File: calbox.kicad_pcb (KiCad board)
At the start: 2 copper layers, 101.6 x 76.2 mm, 68 parts, among them P1 BNC, P2 CONN_01X01, P3 CONN_01X01, Q1 Q_NPN_BEC, SW1 SW_Rotary12, SW2 SW_Rotary12, SW3 SW_SPDT, SW4 SW_Rotary12, SW5 SW_DPST_NKK_M2021, U1 74LVC161, U10 74LVC161, U11 74LVC74, U12 74LVC14, U13 LM317_SOT223_4pin, U14 LM317_SOT223_4pin, U2 74LVC161, U3 74LVC161, U4 74LVC161, U5 74LVC00, U6 74LVC161, U7 74LVC161, U8 74LVC00, U9 74LVC74, X1 ACHL_XO

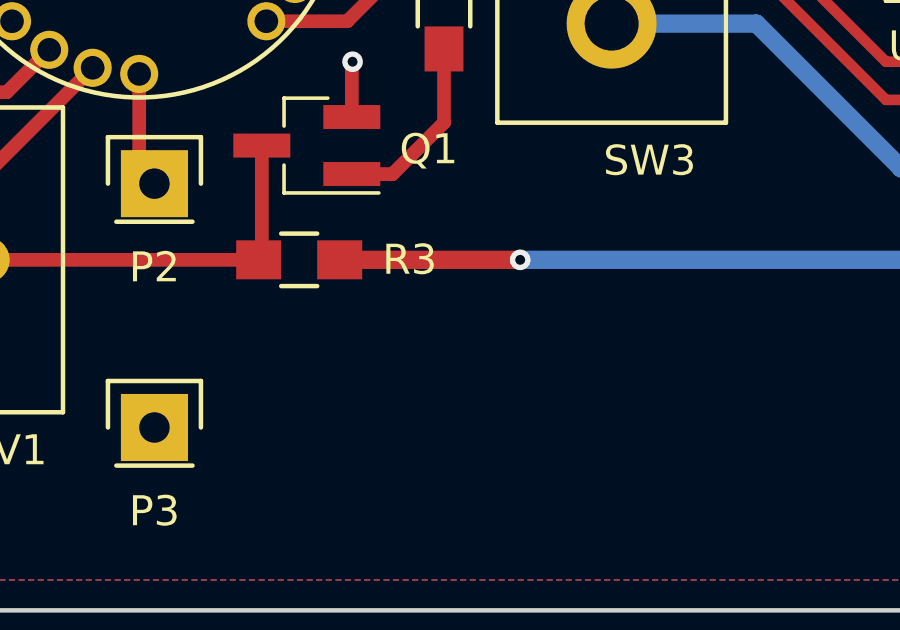
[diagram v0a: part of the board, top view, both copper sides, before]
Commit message: Added bypass capacitor to +12V line
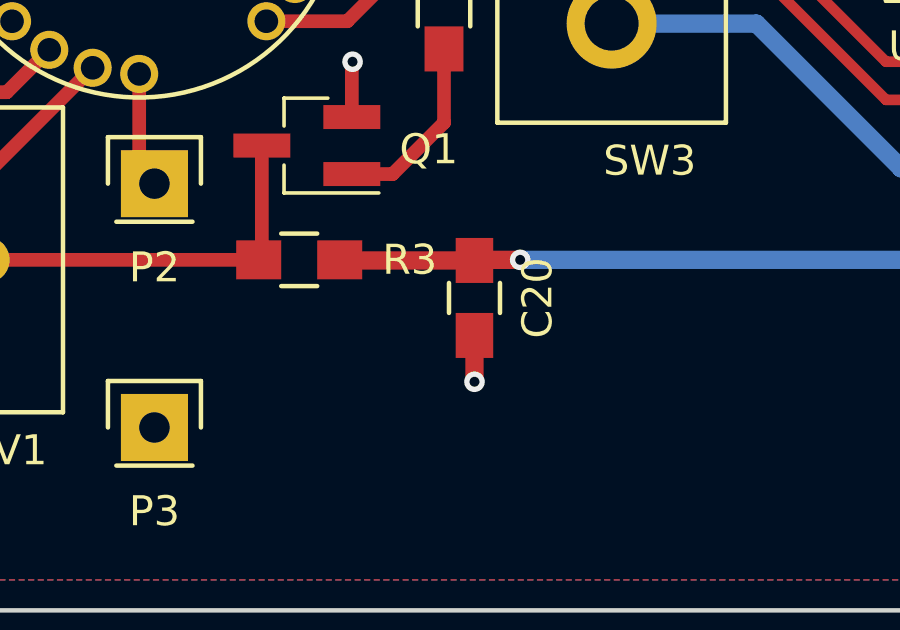
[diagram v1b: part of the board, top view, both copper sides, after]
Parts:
- added C20: 6.8u, Capacitors_SMD:C_0805_HandSoldering, F.Cu at (107.7, 152.1)
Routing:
- net GND: track 129.9 -> 131.5 mm, vias 36 -> 37
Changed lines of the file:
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@@
 (kicad_pcb (version 4) (host pcbnew 4.0.5)
   (general
-    (links 238)
+    (links 240)
     (no_connects 0)
-    (area 65.964999 85.771 169.139239 162.635001)
+    (area 65.964999 86.284999 167.715001 162.635001)
     (thickness 1.6)
     (drawings 4)
-    (tracks 729)
+    (tracks 734)
     (zones 0)
-    (modules 68)
+    (modules 69)
     (nets 99)
   )
@@
   (layers
     (0 F.Cu signal)
-    (31 B.Cu signal)
+    (31 B.Cu signal hide)
     (33 F.Adhes user)
     (35 F.Paste user)
@@
   )
   (setup
-    (last_trace_width 0.3048)
+    (last_trace_width 0.6096)
     (user_trace_width 0.3048)
     (user_trace_width 0.3556)
@@
     )
   )
+  (module Capacitors_SMD:C_0805_HandSoldering (layer F.Cu)
+    (at 107.696 152.146 270)
+    (descr "Capacitor SMD 0805, hand soldering")
+    (tags "capacitor 0805")
+    (attr smd)
+    (fp_text reference C20 (at 0 -2.1 270) (layer F.SilkS)
+      (effects (font (size 1 1) (thickness 0.15)))
+    )
+    (fp_text value 6.8u (at 0 2.1 270) (layer F.Fab)
+      (effects (font (size 1 1) (thickness 0.15)))
+    )
+    (fp_line (start -1 0.625) (end -1 -0.625) (layer F.Fab) (width 0.15))
+    (fp_line (start 1 0.625) (end -1 0.625) (layer F.Fab) (width 0.15))
+    (fp_line (start 1 -0.625) (end 1 0.625) (layer F.Fab) (width 0.15))
+    (fp_line (start -1 -0.625) (end 1 -0.625) (layer F.Fab) (width 0.15))
+    (fp_line (start -2.3 -1) (end 2.3 -1) (layer F.CrtYd) (width 0.05))
+    (fp_line (start -2.3 1) (end 2.3 1) (layer F.CrtYd) (width 0.05))
+    (fp_line (start -2.3 -1) (end -2.3 1) (layer F.CrtYd) (width 0.05))
+    (fp_line (start 2.3 -1) (end 2.3 1) (layer F.CrtYd) (width 0.05))
+    (fp_line (start 0.5 -0.85) (end -0.5 -0.85) (layer F.SilkS) (width 0.15))
+    (fp_line (start -0.5 0.85) (end 0.5 0.85) (layer F.SilkS) (width 0.15))
+    (pad 1 smd rect (at -1.25 0 270) (size 1.5 1.25) (layers F.Cu F.Paste F.Mask)
+      (net 7 +12V))
+    (pad 2 smd rect (at 1.25 0 270) (size 1.5 1.25) (layers F.Cu F.Paste F.Mask)
+      (net 3 GND))
+    (model Capacitors_SMD.3dshapes/C_0805_HandSoldering.wrl
+      (at (xyz 0 0 0))
+      (scale (xyz 1 1 1))
+      (rotate (xyz 0 0 0))
+    )
+  )
   (gr_line (start 167.64 162.56) (end 66.04 162.56) (angle 90) (layer Edge.Cuts) (width 0.15))
   (gr_line (start 167.64 86.36) (end 167.64 162.56) (angle 90) (layer Edge.Cuts) (width 0.15))
@@
   (segment (start 160.147 99.695) (end 159.004 98.552) (width 0.4572) (layer F.Cu) (net 2))
   (segment (start 163.83 99.695) (end 163.83 93.345) (width 0.4572) (layer F.Cu) (net 2))
+  (segment (start 107.696 153.396) (end 107.696 154.94) (width 0.6096) (layer F.Cu) (net 3))
+  (via (at 107.696 154.94) (size 0.6858) (drill 0.3302) (layers F.Cu B.Cu) (net 3))
   (segment (start 144.86 95.885) (end 144.86 98.425) (width 0.6096) (layer F.Cu) (net 3))
   (segment (start 144.86 98.425) (end 146.511 100.076) (width 0.6096) (layer F.Cu) (net 3))
@@
   (segment (start 164.56 119.5) (end 164.44 119.62) (width 0.4572) (layer F.Cu) (net 6))
   (segment (start 161.29 108.966) (end 161.29 109.22) (width 0.4572) (layer F.Cu) (net 6))
+  (segment (start 107.696 150.896) (end 103.224 150.896) (width 0.6096) (layer F.Cu) (net 7))
+  (segment (start 103.224 150.896) (end 103.204 150.876) (width 0.6096) (layer F.Cu) (net 7))
+  (segment (start 109.22 150.876) (end 107.716 150.876) (width 0.6096) (layer F.Cu) (net 7))
+  (segment (start 107.716 150.876) (end 107.696 150.896) (width 0.6096) (layer F.Cu) (net 7))
   (segment (start 158.77 133.35) (end 158.77 136.886) (width 0.6096) (layer F.Cu) (net 7))
-  (segment (start 158.77 136.886) (end 157.988 137.668) (width 0.6096) (layer F.Cu) (net 7))
-  (via (at 157.988 137.668) (size 0.6858) (drill 0.3302) (layers F.Cu B.Cu) (net 7))
-  (segment (start 157.988 137.668) (end 152.908 142.748) (width 0.6096) (layer B.Cu) (net 7))
-  (segment (start 152.908 142.748) (end 148.844 142.748) (width 0.6096) (layer B.Cu) (net 7))
-  (segment (start 148.844 142.748) (end 140.716 150.876) (width 0.6096) (layer B.Cu) (net 7))
-  (segment (start 140.716 150.876) (end 109.22 150.876) (width 0.6096) (layer B.Cu) (net 7))
   (via (at 109.22 150.876) (size 0.6858) (drill 0.3302) (layers F.Cu B.Cu) (net 7))
-  (segment (start 109.22 150.876) (end 103.204 150.876) (width 0.6096) (layer F.Cu) (net 7))
+  (segment (start 140.716 150.876) (end 109.22 150.876) (width 0.6096) (layer B.Cu) (net 7))
+  (segment (start 148.844 142.748) (end 140.716 150.876) (width 0.6096) (layer B.Cu) (net 7))
+  (segment (start 152.908 142.748) (end 148.844 142.748) (width 0.6096) (layer B.Cu) (net 7))
+  (segment (start 157.988 137.668) (end 152.908 142.748) (width 0.6096) (layer B.Cu) (net 7))
+  (via (at 157.988 137.668) (size 0.6858) (drill 0.3302) (layers F.Cu B.Cu) (net 7))
+  (segment (start 158.77 136.886) (end 157.988 137.668) (width 0.6096) (layer F.Cu) (net 7))
   (segment (start 158.14 121.92) (end 158.14 121.056) (width 0.6096) (layer F.Cu) (net 7))
   (segment (start 158.14 121.056) (end 155.448 118.364) (width 0.6096) (layer F.Cu) (net 7))

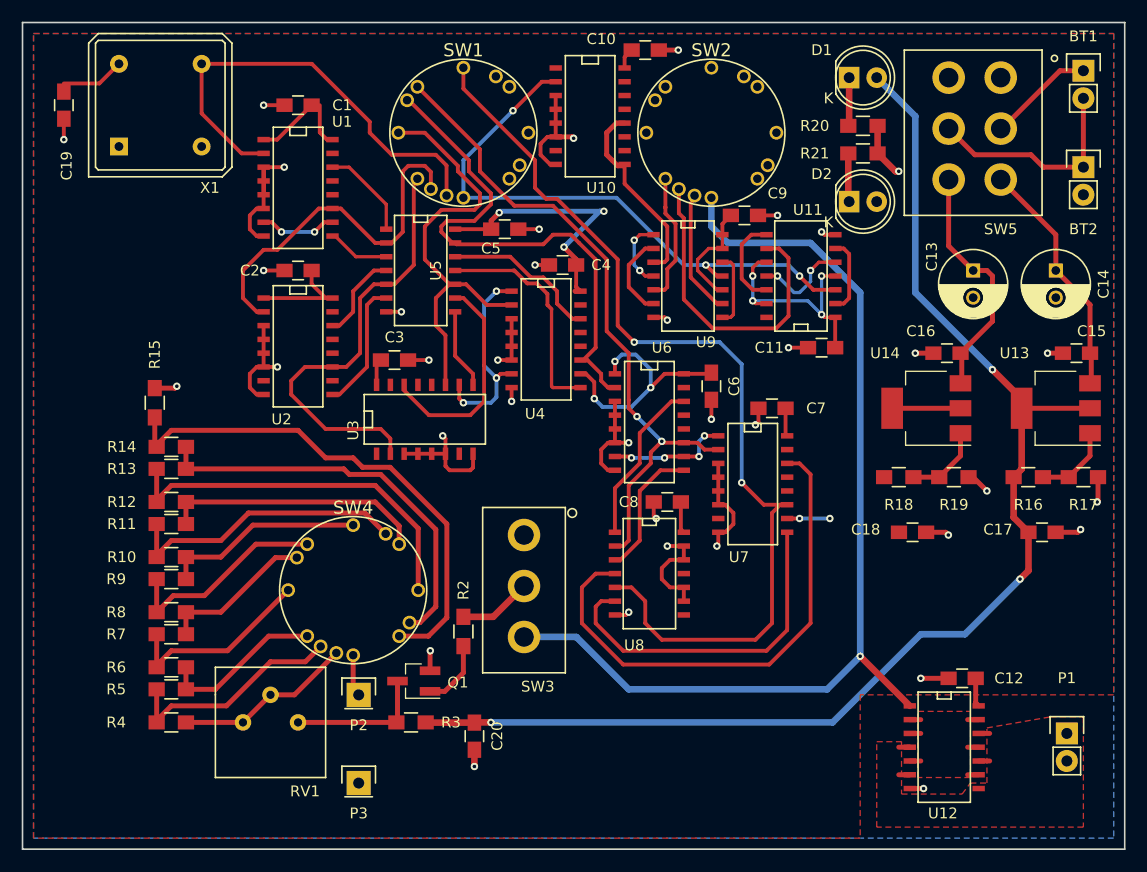
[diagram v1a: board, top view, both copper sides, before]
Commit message: Added testpoints for VCC, 12V, and GND
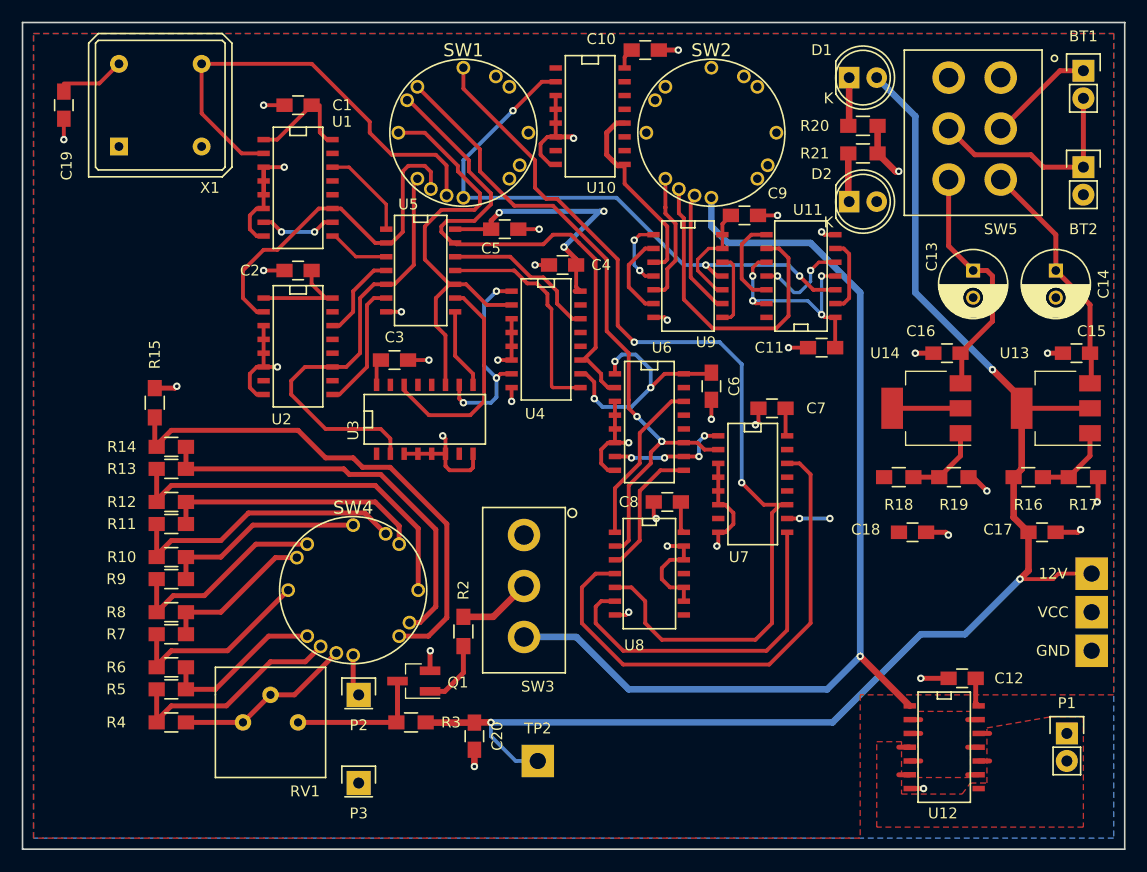
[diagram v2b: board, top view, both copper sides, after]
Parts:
- added 12V: TEST, Measurement_Points:Measurement_Point_Square-TH_Big, F.Cu at (164.6, 137.2)
- added GND: TEST, Measurement_Points:Measurement_Point_Square-TH_Big, F.Cu at (164.6, 144.3)
- added TP2: TEST, Measurement_Points:Measurement_Point_Square-TH_Big, F.Cu at (113.5, 154.4)
- added VCC: TEST, Measurement_Points:Measurement_Point_Square-TH_Big, F.Cu at (164.6, 140.7)
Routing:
- net +12V: track 119.6 -> 132.9 mm
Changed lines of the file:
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@@
 (kicad_pcb (version 4) (host pcbnew 4.0.5)
   (general
-    (links 240)
+    (links 244)
     (no_connects 0)
     (area 65.964999 86.284999 167.715001 162.635001)
     (thickness 1.6)
     (drawings 4)
-    (tracks 734)
+    (tracks 740)
     (zones 0)
-    (modules 69)
+    (modules 73)
     (nets 99)
   )
@@
   (layers
     (0 F.Cu signal)
-    (31 B.Cu signal hide)
+    (31 B.Cu signal)
     (33 F.Adhes user)
     (35 F.Paste user)
@@
   )
   (setup
-    (last_trace_width 0.6096)
+    (last_trace_width 0.3048)
     (user_trace_width 0.3048)
     (user_trace_width 0.3556)
@@
     (tags "CMS SOJ")
     (attr smd)
-    (fp_text reference U5 (at 0 -1.27 270) (layer F.SilkS)
+    (fp_text reference U5 (at -6.096 1.27 360) (layer F.SilkS)
       (effects (font (size 1 1) (thickness 0.15)))
     )
@@
     (descr "Through hole pin header")
     (tags "pin header")
-    (fp_text reference P1 (at 0 -5.1) (layer F.SilkS)
+    (fp_text reference P1 (at 0 -2.794) (layer F.SilkS)
       (effects (font (size 1 1) (thickness 0.15)))
     )
@@
     )
   )
+  (module Measurement_Points:Measurement_Point_Square-TH_Big (layer F.Cu)
+    (at 113.538 154.432)
+    (descr "Mesurement Point, Square, Trough Hole,  3mm x 3mm, Drill 1.5mm,")
+    (tags "Mesurement Point Square Trough Hole 3x3mm Drill 1.5mm")
+    (attr virtual)
+    (fp_text reference TP2 (at 0 -3) (layer F.SilkS)
+      (effects (font (size 1 1) (thickness 0.15)))
+    )
+    (fp_text value TEST (at 0 3) (layer F.Fab)
+      (effects (font (size 1 1) (thickness 0.15)))
+    )
+    (fp_line (start -1.75 -1.75) (end 1.75 -1.75) (layer F.CrtYd) (width 0.05))
+    (fp_line (start 1.75 -1.75) (end 1.75 1.75) (layer F.CrtYd) (width 0.05))
+    (fp_line (start 1.75 1.75) (end -1.75 1.75) (layer F.CrtYd) (width 0.05))
+    (fp_line (start -1.75 1.75) (end -1.75 -1.75) (layer F.CrtYd) (width 0.05))
+    (pad 1 thru_hole rect (at 0 0) (size 3 3) (drill 1.5) (layers *.Cu *.Mask)
+      (net 7 +12V))
+  )
+  (module Measurement_Points:Measurement_Point_Square-TH_Big (layer F.Cu)
+    (at 164.592 144.272)
+    (descr "Mesurement Point, Square, Trough Hole,  3mm x 3mm, Drill 1.5mm,")
+    (tags "Mesurement Point Square Trough Hole 3x3mm Drill 1.5mm")
+    (attr virtual)
+    (fp_text reference GND (at -3.556 0) (layer F.SilkS)
+      (effects (font (size 1 1) (thickness 0.15)))
+    )
+    (fp_text value TEST (at 0 3) (layer F.Fab)
+      (effects (font (size 1 1) (thickness 0.15)))
+    )
+    (fp_line (start -1.75 -1.75) (end 1.75 -1.75) (layer F.CrtYd) (width 0.05))
+    (fp_line (start 1.75 -1.75) (end 1.75 1.75) (layer F.CrtYd) (width 0.05))
+    (fp_line (start 1.75 1.75) (end -1.75 1.75) (layer F.CrtYd) (width 0.05))
+    (fp_line (start -1.75 1.75) (end -1.75 -1.75) (layer F.CrtYd) (width 0.05))
+    (pad 1 thru_hole rect (at 0 0) (size 3 3) (drill 1.5) (layers *.Cu *.Mask)
+      (net 3 GND))
+  )
+  (module Measurement_Points:Measurement_Point_Square-TH_Big (layer F.Cu)
+    (at 164.592 137.16)
+    (descr "Mesurement Point, Square, Trough Hole,  3mm x 3mm, Drill 1.5mm,")
+    (tags "Mesurement Point Square Trough Hole 3x3mm Drill 1.5mm")
+    (attr virtual)
+    (fp_text reference 12V (at -3.556 0) (layer F.SilkS)
+      (effects (font (size 1 1) (thickness 0.15)))
+    )
+    (fp_text value TEST (at 0 3) (layer F.Fab)
+      (effects (font (size 1 1) (thickness 0.15)))
+    )
+    (fp_line (start -1.75 -1.75) (end 1.75 -1.75) (layer F.CrtYd) (width 0.05))
+    (fp_line (start 1.75 -1.75) (end 1.75 1.75) (layer F.CrtYd) (width 0.05))
+    (fp_line (start 1.75 1.75) (end -1.75 1.75) (layer F.CrtYd) (width 0.05))
+    (fp_line (start -1.75 1.75) (end -1.75 -1.75) (layer F.CrtYd) (width 0.05))
+    (pad 1 thru_hole rect (at 0 0) (size 3 3) (drill 1.5) (layers *.Cu *.Mask)
+      (net 7 +12V))
+  )
+  (module Measurement_Points:Measurement_Point_Square-TH_Big (layer F.Cu)
+    (at 164.592 140.716)
+    (descr "Mesurement Point, Square, Trough Hole,  3mm x 3mm, Drill 1.5mm,")
+    (tags "Mesurement Point Square Trough Hole 3x3mm Drill 1.5mm")
+    (attr virtual)
+    (fp_text reference VCC (at -3.556 0) (layer F.SilkS)
+      (effects (font (size 1 1) (thickness 0.15)))
+    )
+    (fp_text value TEST (at 0 3) (layer F.Fab)
+      (effects (font (size 1 1) (thickness 0.15)))
+    )
+    (fp_line (start -1.75 -1.75) (end 1.75 -1.75) (layer F.CrtYd) (width 0.05))
+    (fp_line (start 1.75 -1.75) (end 1.75 1.75) (layer F.CrtYd) (width 0.05))
+    (fp_line (start 1.75 1.75) (end -1.75 1.75) (layer F.CrtYd) (width 0.05))
+    (fp_line (start -1.75 1.75) (end -1.75 -1.75) (layer F.CrtYd) (width 0.05))
+    (pad 1 thru_hole rect (at 0 0) (size 3 3) (drill 1.5) (layers *.Cu *.Mask)
+      (net 4 VCC))
+  )
   (gr_line (start 167.64 162.56) (end 66.04 162.56) (angle 90) (layer Edge.Cuts) (width 0.15))
   (gr_line (start 167.64 86.36) (end 167.64 162.56) (angle 90) (layer Edge.Cuts) (width 0.15))
@@
   (segment (start 164.56 119.5) (end 164.44 119.62) (width 0.4572) (layer F.Cu) (net 6))
   (segment (start 161.29 108.966) (end 161.29 109.22) (width 0.4572) (layer F.Cu) (net 6))
+  (segment (start 157.988 137.668) (end 161.036 137.668) (width 0.3556) (layer F.Cu) (net 7))
+  (segment (start 161.036 137.668) (end 161.544 137.16) (width 0.3556) (layer F.Cu) (net 7))
+  (segment (start 161.544 137.16) (end 164.592 137.16) (width 0.3556) (layer F.Cu) (net 7))
+  (segment (start 109.22 150.876) (end 109.22 152.146) (width 0.3556) (layer B.Cu) (net 7))
+  (segment (start 109.22 152.146) (end 111.506 154.432) (width 0.3556) (layer B.Cu) (net 7))
+  (segment (start 111.506 154.432) (end 113.538 154.432) (width 0.3556) (layer B.Cu) (net 7))
   (segment (start 107.696 150.896) (end 103.224 150.896) (width 0.6096) (layer F.Cu) (net 7))
   (segment (start 103.224 150.896) (end 103.204 150.876) (width 0.6096) (layer F.Cu) (net 7))

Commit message: Updated voltage output divider to use practical resistor values
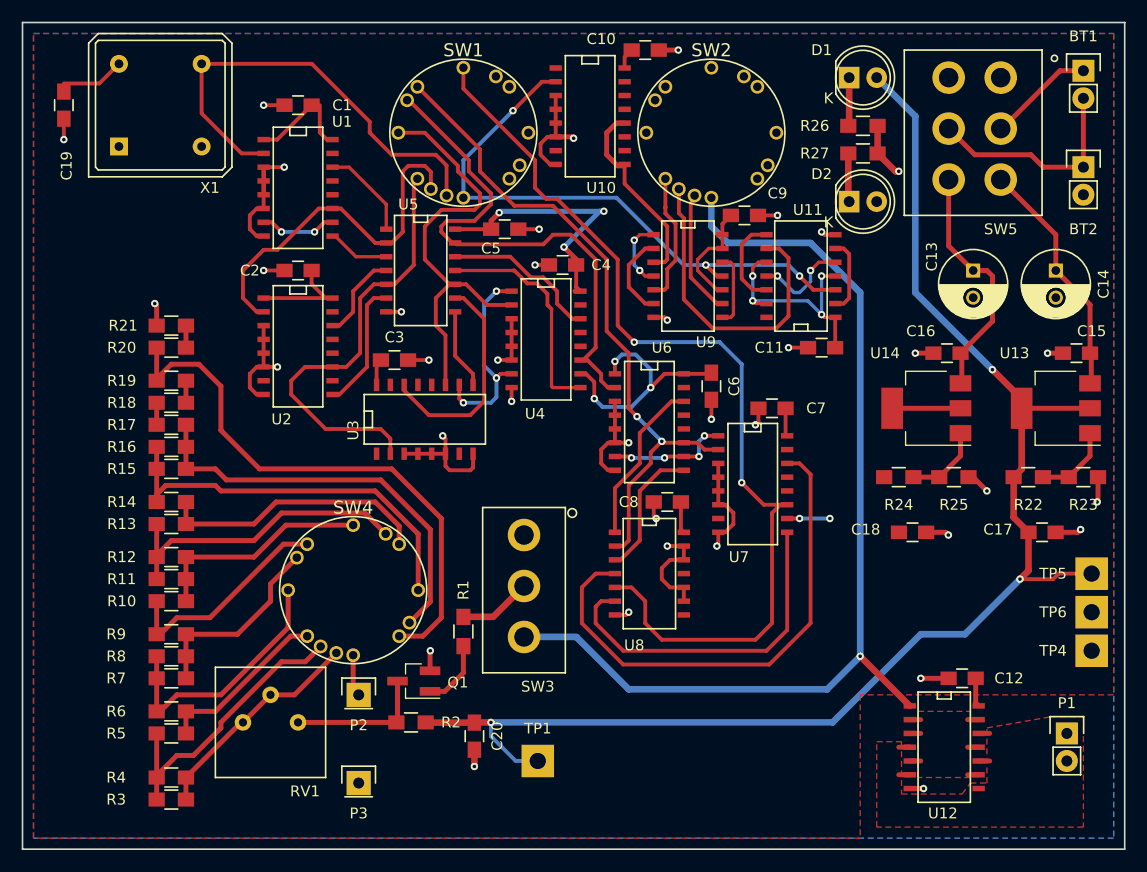
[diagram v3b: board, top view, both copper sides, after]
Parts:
- added R11: 1k, Resistors_SMD:R_0805_HandSoldering, F.Cu at (79.8, 137.7)
- added R15: 100, Resistors_SMD:R_0805_HandSoldering, F.Cu at (79.8, 127.5)
- added R18: 100, Resistors_SMD:R_0805_HandSoldering, F.Cu at (79.8, 121.4)
- added R19: 100, Resistors_SMD:R_0805_HandSoldering, F.Cu at (79.8, 119.4)
- added R20: 100, Resistors_SMD:R_0805_HandSoldering, F.Cu at (79.8, 116.3)
- added R3: 100k, Resistors_SMD:R_0805_HandSoldering, F.Cu at (79.8, 158.0)
- added R7: 10k, Resistors_SMD:R_0805_HandSoldering, F.Cu at (79.8, 146.8)
- R10: renamed from R9; value R -> 1k
- R12: renamed from R10; value R -> 1k
- R13: renamed from R11; value R -> 300
- R14: renamed from R12; value R -> 100
- R16: renamed from R13; value R -> 100
- R17: renamed from R14; value R -> 100
- R21: renamed from R15; value R -> 100
- R4: value R -> 100k
- R5: value R -> 30k
- R6: value R -> 10k
- R8: renamed from R7; value R -> 10k
- R9: renamed from R8; value R -> 3k
- moved R21 7.27 mm to (79.8, 114.3), turned to 180 degrees
- moved R4 5.08 mm to (79.8, 156.0)
- moved R6 4.06 mm to (79.8, 149.9)
- moved R5 4.06 mm to (79.8, 151.9)
- moved R8 2.03 mm to (79.8, 144.8)
- moved R16 2.03 mm to (79.8, 125.5)
- moved R17 2.03 mm to (79.8, 123.4)
- moved R10 2.03 mm to (79.8, 139.7)
- moved R9 2.03 mm to (79.8, 142.7)
- renumbered R2 to R1, R3 to R2, R16 to R22, R17 to R23, R18 to R24, R19 to R25, R20 to R26, R21 to R27, TP2 to TP1, GND to TP4, 12V to TP5, VCC to TP6
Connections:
- R17 pad 2: /voltage_output/2mV_out -> Net-(R17-Pad2)
- R21 pad 1: /voltage_output/2mV_out -> Net-(R20-Pad2)
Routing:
- net /voltage_output/1V_out: track 18.2 -> 24.0 mm
- net /voltage_output/5V_out: track 21.2 -> 26.6 mm
- net /voltage_output/2mV_out: track 47.6 -> 52.0 mm
- net /voltage_output/10V_out: track 16.5 -> 20.7 mm
- net /voltage_output/500mV_out: track 14.3 -> 18.1 mm
- net /voltage_output/50mV_out: track 26.7 -> 29.1 mm
- net /voltage_output/10mV_out: track 35.2 -> 37.4 mm
- net Net-(R18-Pad2): track 0.00 -> 2.03 mm
- net Net-(R20-Pad2): track 0.00 -> 2.03 mm
- net Net-(R17-Pad2): track 0.00 -> 2.03 mm
- net /voltage_output/100mV_out: track 18.7 -> 20.7 mm
- net /voltage_output/200mV_out: track 19.5 -> 20.5 mm
- net /voltage_output/20mV_out: track 24.3 -> 25.1 mm
- net /voltage_output/2V_out: track 15.2 -> 16.1 mm
- net /voltage_output/5mV_out: track 37.5 -> 38.3 mm
